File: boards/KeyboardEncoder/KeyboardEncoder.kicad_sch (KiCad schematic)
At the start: 21 parts, among them J1 Keyboard1, J2 Keyboard1, J3 Encoder, U1 74151, U10 74151, U2 74151, U3 74151, U4 74151, U5 ULN2803A, U6 74151, U7 74151, U8 4069, U9 74151

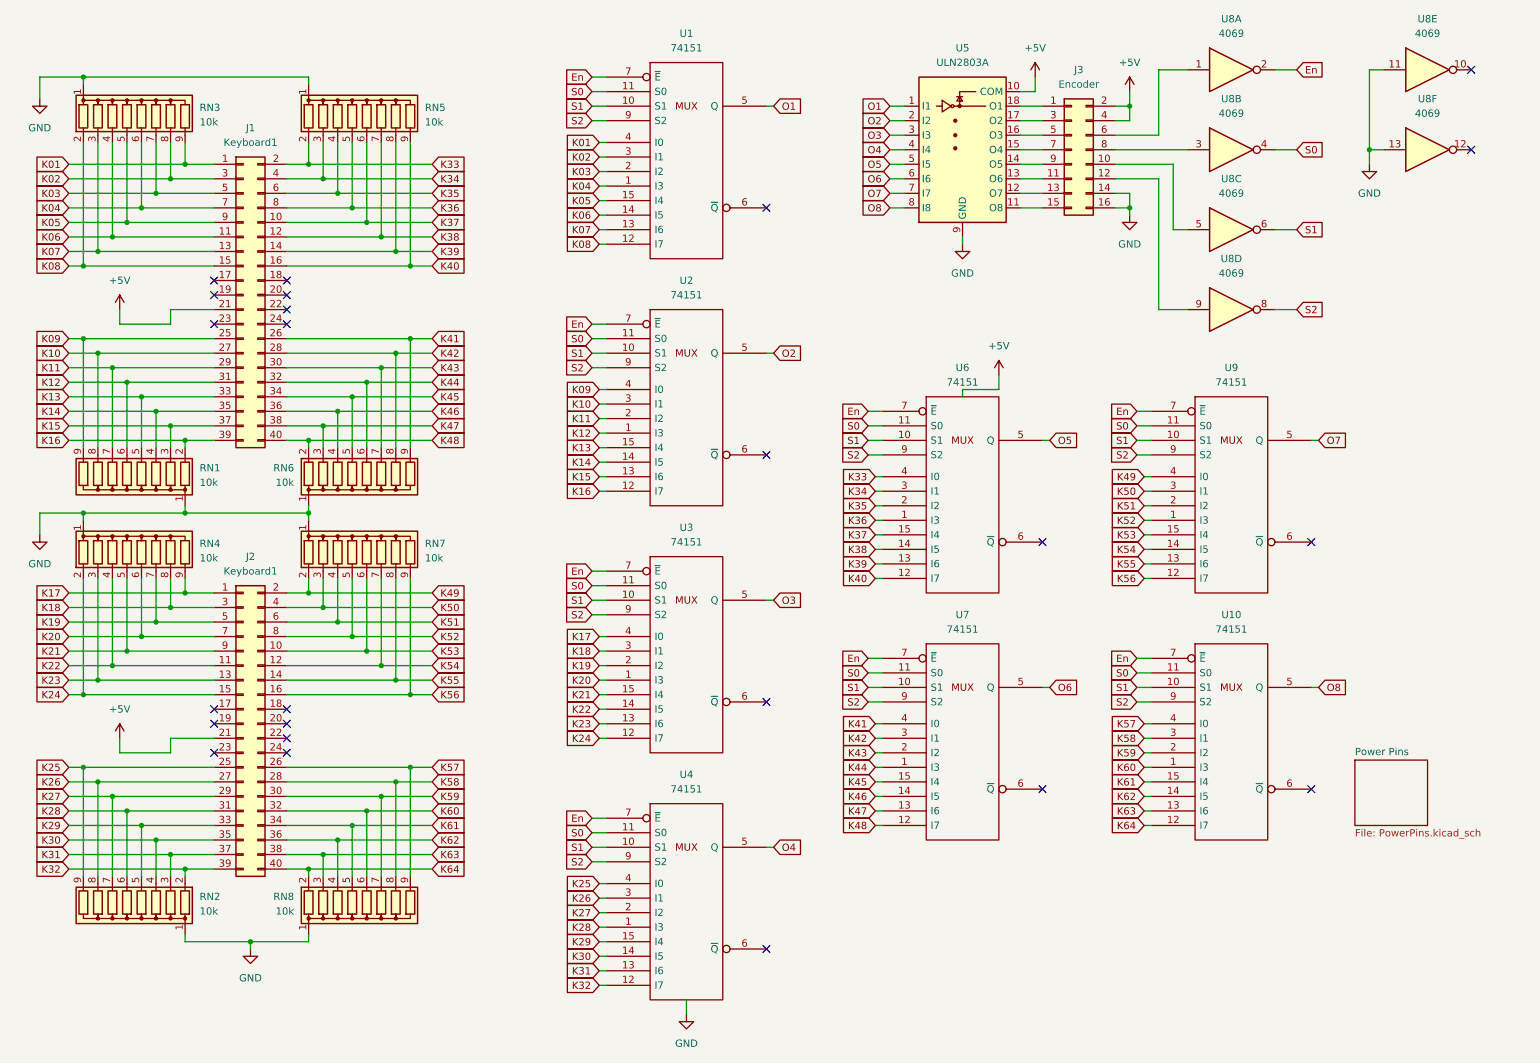
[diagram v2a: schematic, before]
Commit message: Renamed PCBs and updated to KiCAD 7.0
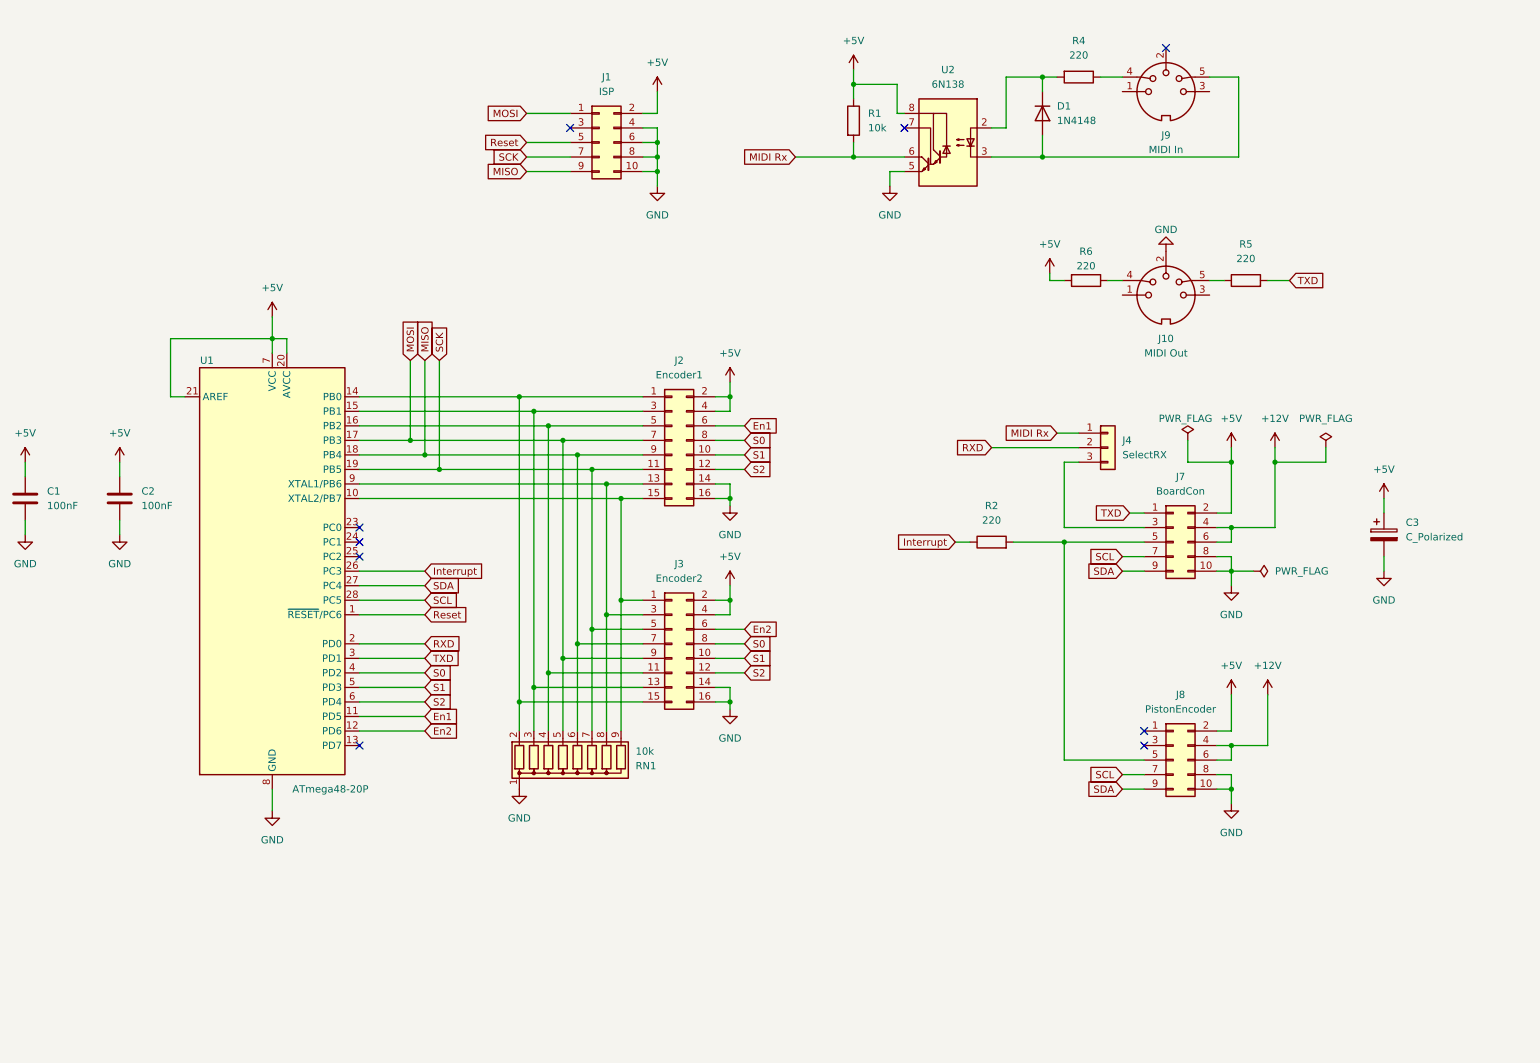
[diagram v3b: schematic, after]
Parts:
- removed J1, J2: Keyboard1, symbol Connector_Generic:Conn_02x20_Odd_Even
- removed RN2, RN3, RN4, RN5, RN6, RN7, RN8: 10k, Resistor_THT:R_Array_SIP9, symbol Device:R_Network08
- removed U1, U10, U2, U3, U4, U6, U7, U9: 74151, symbol 74xx_IEEE:74151
- removed U5: ULN2803A, symbol Transistor_Array:ULN2803A
- removed U8: 4069, symbol 4xxx:4069
- added C1, C2: 100nF, Capacitor_THT:C_Disc_D7.5mm_W2.5mm_P5.00mm, symbol Device:C
- added C3: C_Polarized, Capacitor_THT:CP_Radial_D10.0mm_P5.00mm, symbol Device:C_Polarized
- added D1: 1N4148, Diode_THT:D_DO-35_SOD27_P7.62mm_Horizontal, symbol Diode:1N4148
- added J1: ISP, Connector_IDC:IDC-Header_2x05_P2.54mm_Vertical, symbol Connector_Generic:Conn_02x05_Odd_Even
- added J10: MIDI Out, symbol Connector:DIN-5_180degree
- added J2: Encoder1, Connector_IDC:IDC-Header_2x08_P2.54mm_Vertical, symbol Connector_Generic:Conn_02x08_Odd_Even
- added J4: SelectRX, Connector_PinHeader_2.54mm:PinHeader_1x03_P2.54mm_Vertical, symbol Connector_Generic:Conn_01x03
- added J7: BoardCon, Connector_IDC:IDC-Header_2x05_P2.54mm_Vertical, symbol Connector_Generic:Conn_02x05_Odd_Even
- added J8: PistonEncoder, Connector_IDC:IDC-Header_2x05_P2.54mm_Vertical, symbol Connector_Generic:Conn_02x05_Odd_Even
- added J9: MIDI In, symbol Connector:DIN-5_180degree
- added R1: 10k, Resistor_THT:R_Axial_DIN0204_L3.6mm_D1.6mm_P2.54mm_Vertical, symbol Device:R
- added R2, R4, R5, R6: 220, Resistor_THT:R_Axial_DIN0204_L3.6mm_D1.6mm_P2.54mm_Vertical, symbol Device:R
- added U1: ATmega48-20P, Package_DIP:DIP-28_W7.62mm, symbol MCU_Microchip_ATmega:ATmega48-20P
- added U2: 6N138, Package_DIP:DIP-8_W7.62mm, symbol Isolator:6N138
- J3: value Encoder -> Encoder2; footprint (none) -> Connector_IDC:IDC-Header_2x08_P2.54mm_Vertical
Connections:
- net K09 is gone; now on an unnamed net: RN1.9 (R8)
- net K10 is gone; now on an unnamed net: RN1.8 (R7)
- net K11 is gone; now on net SCK: RN1.7 (R6)
- net K12 is gone; now on net MISO: RN1.6 (R5)
- net K13 is gone; now on net MOSI: RN1.5 (R4)
- net K14 is gone; now on an unnamed net: RN1.4 (R3)
- net K15 is gone; now on an unnamed net: RN1.3 (R2)
- net K16 is gone; now on an unnamed net: RN1.2 (R1)
- net +5V: now also C1.1, C2.1, C3.1, J1.2 (Pin_2), J2.2 (Pin_2), J2.4 (Pin_4), J7.2 (Pin_2), J8.2 (Pin_2), R1.1, R6.2, U1.20 (AVCC), U1.21 (AREF), U1.7 (VCC), U2.8 (VCC)
- net GND: now also C1.2, C2.2, C3.2, J1.10 (Pin_10), J1.4 (Pin_4), J1.6 (Pin_6), J1.8 (Pin_8), J10.2, J2.14 (Pin_14), J2.16 (Pin_16), J7.10 (Pin_10), J7.8 (Pin_8), J8.10 (Pin_10), J8.8 (Pin_8), U1.22 (GND), U1.8 (GND), U2.5 (GND)
- net S0: now also J3.8 (Pin_8), J2.8 (Pin_8), U1.4 (PD2)
- net S1: now also J3.10 (Pin_10), J2.10 (Pin_10), U1.5 (PD3)
- net S2: now also J3.12 (Pin_12), J2.12 (Pin_12), U1.6 (PD4)
- net at J3.15 (Pin_15): now also J2.1 (Pin_1), U1.14 (PB0)
- net at J3.13 (Pin_13): now also J2.3 (Pin_3), U1.15 (PB1)
- net at J3.11 (Pin_11): now also J2.5 (Pin_5), U1.16 (PB2)
- net MOSI: now reaches J3.9 (Pin_9)
- net MOSI: now also J1.1 (Pin_1), J2.7 (Pin_7), U1.17 (PB3)
- net MISO: now reaches J3.7 (Pin_7)
- net MISO: now also J1.9 (Pin_9), J2.9 (Pin_9), U1.18 (PB4)
- net SCK: now reaches J3.5 (Pin_5)
- net SCK: now also J1.7 (Pin_7), J2.11 (Pin_11), U1.19 (PB5)
- net at J3.3 (Pin_3): now also J2.13 (Pin_13), U1.9 (XTAL1/PB6)
- net at J3.1 (Pin_1): now also J2.15 (Pin_15), U1.10 (XTAL2/PB7)
- net En2: now reaches J3.6 (Pin_6)
- net En2: now also U1.12 (PD6)
- new net: J10.4, R6.1
- new net: J10.5, R5.1
- new net: D1.1 (K), R4.2, U2.2 (C1)
- new net: D1.2 (A), J9.5, U2.3 (C2)
- new net: J9.4, R4.1
- new net: J4.3 (Pin_3), J7.3 (Pin_3)
- new net: J7.5 (Pin_5), J8.5 (Pin_5), R2.2
- new net +12V: J7.4 (Pin_4), J7.6 (Pin_6), J8.4 (Pin_4), J8.6 (Pin_6)
- new net En1: J2.6 (Pin_6), U1.11 (PD5)
- new net Interrupt: R2.1, U1.26 (PC3)
- new net MIDI Rx: J4.1 (Pin_1), R1.2, U2.6 (VO2)
- new net RXD: J4.2 (Pin_2), U1.2 (PD0)
- new net Reset: J1.5 (Pin_5), U1.1 (~{RESET}/PC6)
- new net SCL: J7.7 (Pin_7), J8.7 (Pin_7), U1.28 (PC5)
- new net SDA: J7.9 (Pin_9), J8.9 (Pin_9), U1.27 (PC4)
- new net TXD: J7.1 (Pin_1), R5.2, U1.3 (PD1)
- no-connect marks 24 -> 9
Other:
- removed sheet Power Pins

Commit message: PCB layout for keyboard scanner and piston encoder
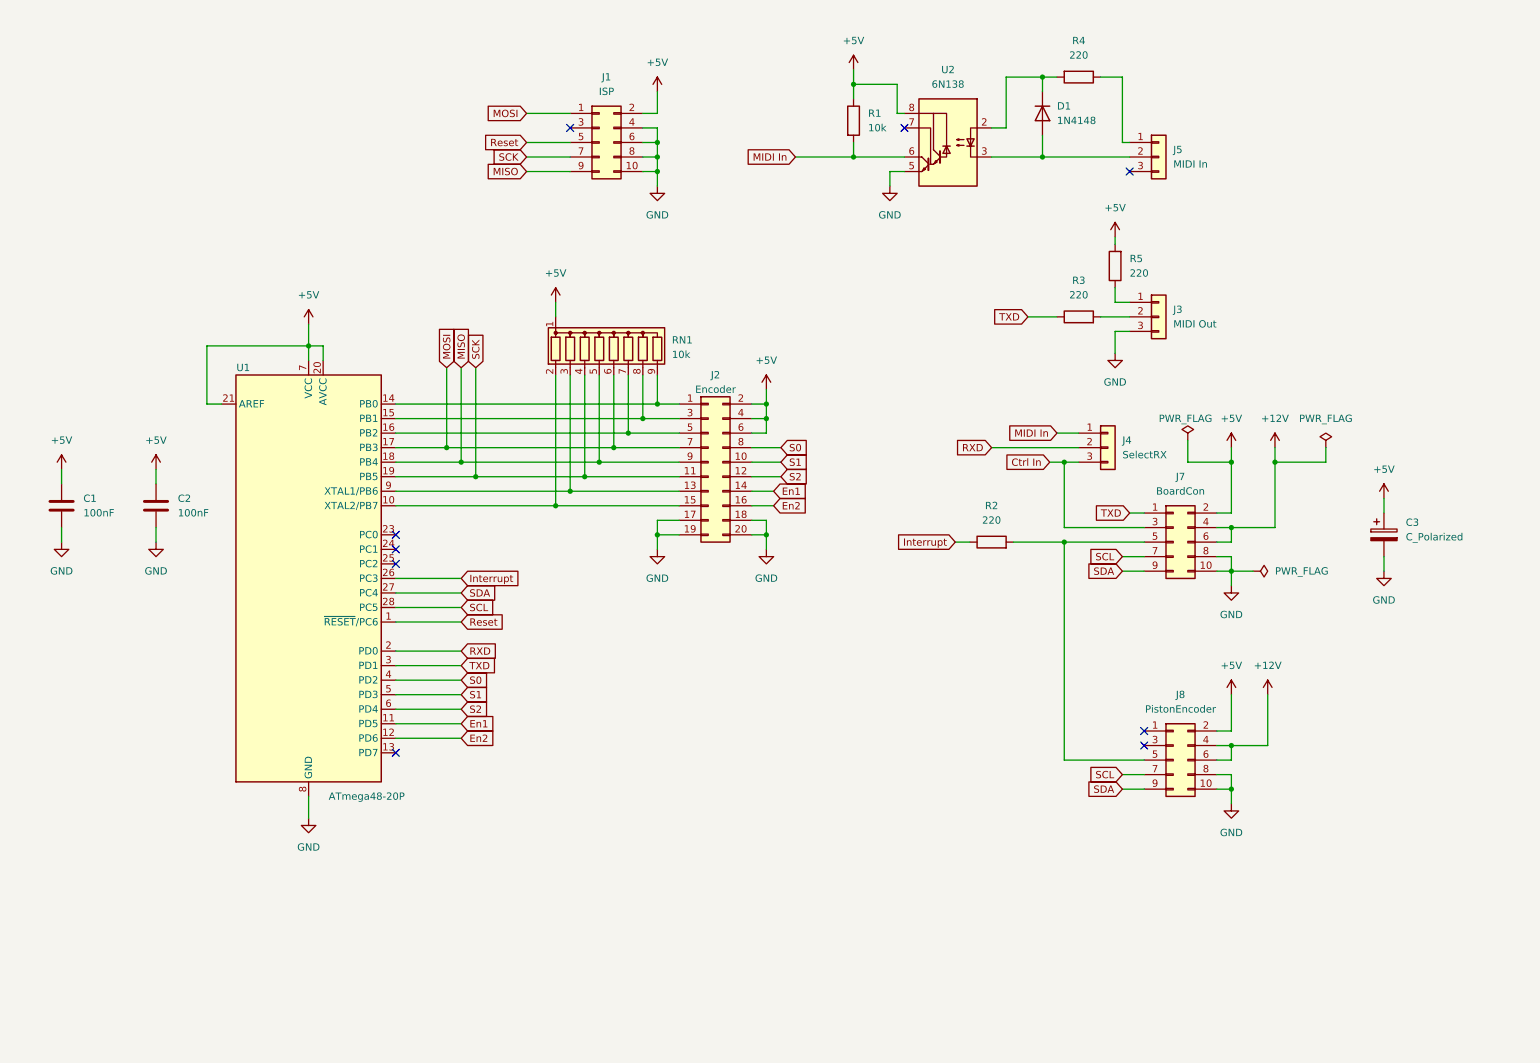
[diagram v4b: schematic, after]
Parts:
- removed J10: MIDI Out, symbol Connector:DIN-5_180degree
- removed J2: Encoder1, Connector_IDC:IDC-Header_2x08_P2.54mm_Vertical, symbol Connector_Generic:Conn_02x08_Odd_Even
- removed J3: Encoder2, Connector_IDC:IDC-Header_2x08_P2.54mm_Vertical, symbol Connector_Generic:Conn_02x08_Odd_Even
- removed J9: MIDI In, symbol Connector:DIN-5_180degree
- removed R6: 220, Resistor_THT:R_Axial_DIN0204_L3.6mm_D1.6mm_P2.54mm_Vertical, symbol Device:R
- added J2: Encoder, Connector_IDC:IDC-Header_2x10_P2.54mm_Vertical, symbol Connector_Generic:Conn_02x10_Odd_Even
- added J3: MIDI Out, Connector_PinHeader_2.54mm:PinHeader_1x03_P2.54mm_Vertical, symbol Connector_Generic:Conn_01x03
- added J5: MIDI In, Connector_PinHeader_2.54mm:PinHeader_1x03_P2.54mm_Vertical, symbol Connector_Generic:Conn_01x03
- added R3: 220, Resistor_THT:R_Axial_DIN0204_L3.6mm_D1.6mm_P2.54mm_Vertical, symbol Device:R
- C1, C2: footprint Capacitor_THT:C_Disc_D7.5mm_W2.5mm_P5.00mm -> Capacitor_THT:C_Disc_D4.3mm_W1.9mm_P5.00mm
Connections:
- net +5V: now also R5.2, RN1.1 (common), J2.2 (Pin_2), J2.4 (Pin_4), J2.6 (Pin_6)
- net En1: now also J2.14 (Pin_14)
- net En2: now also J2.16 (Pin_16)
- net GND: now also J2.17 (Pin_17), J2.18 (Pin_18), J2.19 (Pin_19), J2.20 (Pin_20), J3.3 (Pin_3); no longer RN1.1 (common)
- net MISO: now also RN1.5 (R4), J2.9 (Pin_9); no longer RN1.6 (R5)
- net MOSI: now also RN1.6 (R5), J2.7 (Pin_7); no longer RN1.5 (R4)
- net S0: now also J2.8 (Pin_8)
- net S1: now also J2.10 (Pin_10)
- net S2: now also J2.12 (Pin_12)
- net SCK: now also RN1.4 (R3), J2.11 (Pin_11); no longer RN1.7 (R6)
- net TXD: now also R3.1; no longer R5.2
- net at R5.1: now also J3.1 (Pin_1)
- net at D1.2 (A), U2.3 (C2): now also J5.2 (Pin_2)
- net at U1.10 (XTAL2/PB7): now also RN1.2 (R1), J2.15 (Pin_15); no longer RN1.9 (R8)
- net at U1.16 (PB2): now also RN1.7 (R6), J2.5 (Pin_5); no longer RN1.4 (R3)
- net at U1.15 (PB1): now also RN1.8 (R7), J2.3 (Pin_3); no longer RN1.3 (R2)
- net at U1.14 (PB0): now also RN1.9 (R8), J2.1 (Pin_1); no longer RN1.2 (R1)
- net at U1.9 (XTAL1/PB6): now also RN1.3 (R2), J2.13 (Pin_13); no longer RN1.8 (R7)
- net at R4.1: now also J5.1 (Pin_1)
- net Ctrl In: now reaches J4.3 (Pin_3), J7.3 (Pin_3)
- net MIDI Rx renamed MIDI In
- new net: J3.2 (Pin_2), R3.2

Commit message: Added output buffer to MIDI outputs
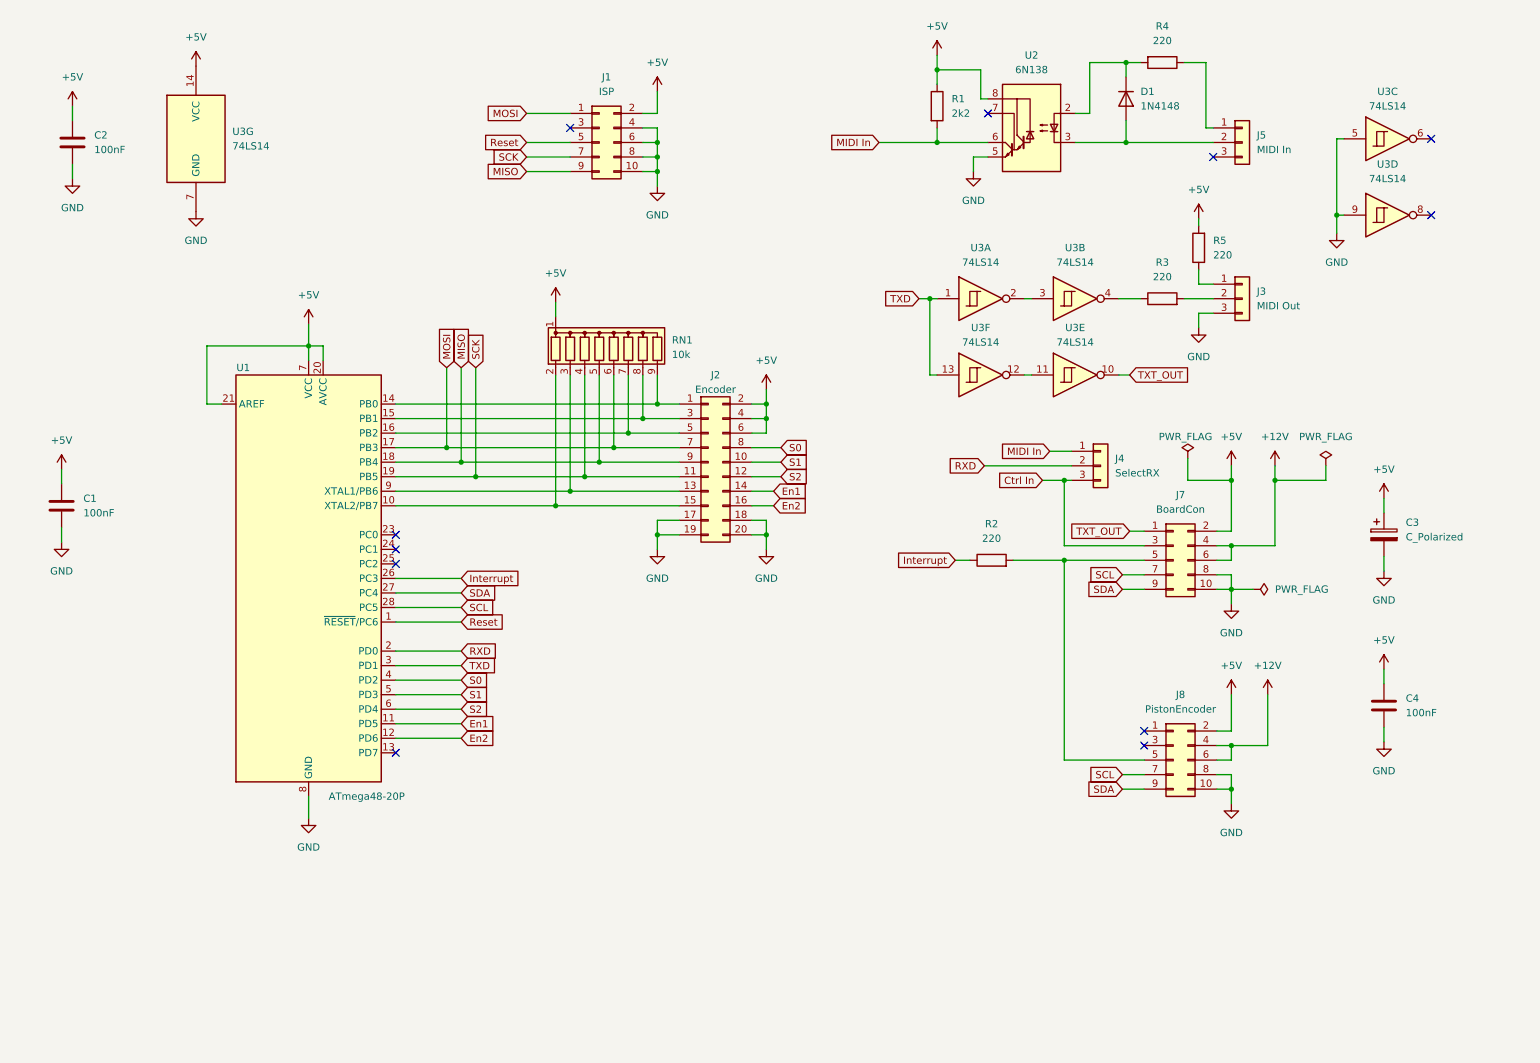
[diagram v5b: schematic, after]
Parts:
- added C4: 100nF, Capacitor_THT:C_Disc_D4.3mm_W1.9mm_P5.00mm, symbol Device:C
- added U3: 74LS14, symbol 74xx:74LS14
- R1: value 10k -> 2k2
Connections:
- net +5V: now also C4.1, U3.14 (VCC)
- net GND: now also C4.2, U3.5, U3.7 (GND), U3.9
- net TXD: now also U3.1, U3.13; no longer J7.1 (Pin_1), R3.1
- new net: U3.2, U3.3
- new net: R3.1, U3.4
- new net: U3.11, U3.12
- new net TXT_OUT: J7.1 (Pin_1), U3.10
- no-connect marks 9 -> 11
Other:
- moved on the sheet: C2, D1, J3, J4, J5, J7, R1, R2, R3, R4, R5, U2
